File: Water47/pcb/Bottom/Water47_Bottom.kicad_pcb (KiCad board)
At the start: 2 copper layers, 260 x 76.5 mm, 5 parts, among them U1 MOUDLE-SEEEDUINO-XIAO

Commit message: feat: change mounting spacer to hex
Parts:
- H1, H2, H3, H4: footprint kbd_Hole:m2_Screw_Hole -> kbd_Hole:m2_Spacer_Hole_hex
- turned H1 to 90 degrees
- turned H2 to 90 degrees
- turned H3 to 90 degrees
- turned H4 to 90 degrees
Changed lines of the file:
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@@
       (net 13 "+5V") (pinfunction "5V") (pintype "passive"))
   )
-  (footprint "kbd_Hole:m2_Screw_Hole" (layer "F.Cu")
-    (at 85 87.2)
-    (descr "Mounting Hole 2.2mm, no annular, M2")
-    (tags "mounting hole 2.2mm no annular m2")
-    (property "Sheetfile" "Water47_Bottom.kicad_sch")
-    (property "Sheetname" "")
-    (autoplace_cost90 1)
-    (attr exclude_from_pos_files)
-    (fp_text reference "H1" (at 0 -3.2) (layer "F.Fab")
-      (effects (font (size 1 1) (thickness 0.15)))
-    )
-    (fp_text value "MountingHole" (at 0 3.2) (layer "F.Fab") hide
-      (effects (font (size 1 1) (thickness 0.15)))
-    )
-    (fp_text user "${REFERENCE}" (at 0.3 0) (layer "F.Fab") hide
-      (effects (font (size 1 1) (thickness 0.15)))
-    )
-    (fp_circle (center 0 0) (end 2.2 0) (layer "Cmts.User") (width 0.15) (fill none))
-    (fp_circle (center 0 0) (end 2.45 0) (layer "F.CrtYd") (width 0.05) (fill none))
-    (pad "" np_thru_hole circle locked (at 0 0) (size 2.2 2.2) (drill 2.2) (layers *.Cu *.Mask))
-  )
-  (footprint "kbd_Hole:m2_Screw_Hole" (layer "F.Cu")
-    (at 85 155.7)
+  (footprint "kbd_Hole:m2_Spacer_Hole_hex" (layer "F.Cu")
+    (at 85 87.2 90)
     (descr "Mounting Hole 2.2mm, no annular, M2")
     (tags "mounting hole 2.2mm no annular m2")
@@
     (property "Sheetname" "")
     (attr exclude_from_pos_files)
-    (fp_text reference "H2" (at 0 -3.2) (layer "F.Fab")
+    (fp_text reference "H1" (at 0 -3.2 90) (layer "F.Fab")
       (effects (font (size 1 1) (thickness 0.15)))
     )
-    (fp_text value "MountingHole" (at 0 3.2) (layer "F.Fab") hide
+    (fp_text value "MountingHole" (at 0 3.2 90) (layer "F.Fab")
       (effects (font (size 1 1) (thickness 0.15)))
     )
-    (fp_text user "${REFERENCE}" (at 0.3 0) (layer "F.Fab") hide
-      (effects (font (size 1 1) (thickness 0.15)))
-    )
-    (fp_circle (center 0 0) (end 2.2 0) (layer "Cmts.User") (width 0.15) (fill none))
-    (fp_circle (center 0 0) (end 2.45 0) (layer "F.CrtYd") (width 0.05) (fill none))
-    (pad "" np_thru_hole circle locked (at 0 0) (size 2.2 2.2) (drill 2.2) (layers *.Cu *.Mask))
+    (fp_line (start 1.2 -2.15) (end -1.2 -2.15) (layer "Edge.Cuts") (width 0.1))
+    (fp_line (start -1.2 2.15) (end 1.2 2.15) (layer "Edge.Cuts") (width 0.1))
+    (fp_line (start -1.2 -2.15) (end -2.4 0) (layer "Edge.Cuts") (width 0.1))
+    (fp_line (start -2.4 0) (end -1.2 2.15) (layer "Edge.Cuts") (width 0.1))
+    (fp_line (start 1.2 2.15) (end 2.4 0) (layer "Edge.Cuts") (width 0.1))
+    (fp_line (start 2.4 0) (end 1.2 -2.15) (layer "Edge.Cuts") (width 0.1))
   )
-  (footprint "kbd_Hole:m2_Screw_Hole" (layer "F.Cu")
-    (at 339 155.7)
+  (footprint "kbd_Hole:m2_Spacer_Hole_hex" (layer "F.Cu")
+    (at 85 155.7 90)
     (descr "Mounting Hole 2.2mm, no annular, M2")
     (tags "mounting hole 2.2mm no annular m2")
@@
     (property "Sheetname" "")
     (attr exclude_from_pos_files)
-    (fp_text reference "H4" (at 0 -3.2) (layer "F.Fab") hide
+    (fp_text reference "H2" (at 0 -3.2 90) (layer "F.Fab")
       (effects (font (size 1 1) (thickness 0.15)))
     )
-    (fp_text value "MountingHole" (at 0 3.2) (layer "F.Fab") hide
+    (fp_text value "MountingHole" (at 0 3.2 90) (layer "F.Fab")
       (effects (font (size 1 1) (thickness 0.15)))
     )
-    (fp_text user "${REFERENCE}" (at 0.3 0) (layer "F.Fab") hide
-      (effects (font (size 1 1) (thickness 0.15)))
-    )
-    (fp_circle (center 0 0) (end 2.2 0) (layer "Cmts.User") (width 0.15) (fill none))
-    (fp_circle (center 0 0) (end 2.45 0) (layer "F.CrtYd") (width 0.05) (fill none))
-    (pad "" np_thru_hole circle locked (at 0 0) (size 2.2 2.2) (drill 2.2) (layers *.Cu *.Mask))
+    (fp_line (start 1.2 -2.15) (end -1.2 -2.15) (layer "Edge.Cuts") (width 0.1))
+    (fp_line (start 1.2 2.15) (end 2.4 0) (layer "Edge.Cuts") (width 0.1))
+    (fp_line (start 2.4 0) (end 1.2 -2.15) (layer "Edge.Cuts") (width 0.1))
+    (fp_line (start -1.2 -2.15) (end -2.4 0) (layer "Edge.Cuts") (width 0.1))
+    (fp_line (start -1.2 2.15) (end 1.2 2.15) (layer "Edge.Cuts") (width 0.1))
+    (fp_line (start -2.4 0) (end -1.2 2.15) (layer "Edge.Cuts") (width 0.1))
   )
-  (footprint "kbd_Hole:m2_Screw_Hole" (layer "F.Cu")
-    (at 339 87.2)
+  (footprint "kbd_Hole:m2_Spacer_Hole_hex" (layer "F.Cu")
+    (at 339 155.7 90)
     (descr "Mounting Hole 2.2mm, no annular, M2")
     (tags "mounting hole 2.2mm no annular m2")
@@
     (property "Sheetname" "")
     (attr exclude_from_pos_files)
-    (fp_text reference "H3" (at 0 -3.2) (layer "F.Fab")
+    (fp_text reference "H4" (at 0 -3.2 90) (layer "F.Fab")
       (effects (font (size 1 1) (thickness 0.15)))
     )
-    (fp_text value "MountingHole" (at 0 3.2) (layer "F.Fab")
+    (fp_text value "MountingHole" (at 0 3.2 90) (layer "F.Fab")
       (effects (font (size 1 1) (thickness 0.15)))
     )
-    (fp_text user "${REFERENCE}" (at 0.3 0) (layer "F.Fab") hide
+    (fp_line (start 1.2 2.15) (end 2.4 0) (layer "Edge.Cuts") (width 0.1))
+    (fp_line (start 1.2 -2.15) (end -1.2 -2.15) (layer "Edge.Cuts") (width 0.1))
+    (fp_line (start -1.2 2.15) (end 1.2 2.15) (layer "Edge.Cuts") (width 0.1))
+    (fp_line (start 2.4 0) (end 1.2 -2.15) (layer "Edge.Cuts") (width 0.1))
+    (fp_line (start -1.2 -2.15) (end -2.4 0) (layer "Edge.Cuts") (width 0.1))
+    (fp_line (start -2.4 0) (end -1.2 2.15) (layer "Edge.Cuts") (width 0.1))
+  )
+  (footprint "kbd_Hole:m2_Spacer_Hole_hex" (layer "F.Cu")
+    (at 339 87.2 90)
+    (descr "Mounting Hole 2.2mm, no annular, M2")
+    (tags "mounting hole 2.2mm no annular m2")
+    (property "Sheetfile" "Water47_Bottom.kicad_sch")
+    (property "Sheetname" "")
+    (attr exclude_from_pos_files)
+    (fp_text reference "H3" (at 0 -3.2 90) (layer "F.Fab")
       (effects (font (size 1 1) (thickness 0.15)))
     )
-    (fp_circle (center 0 0) (end 2.2 0) (layer "Cmts.User") (width 0.15) (fill none))
-    (fp_circle (center 0 0) (end 2.45 0) (layer "F.CrtYd") (width 0.05) (fill none))
-    (pad "" np_thru_hole circle locked (at 0 0) (size 2.2 2.2) (drill 2.2) (layers *.Cu *.Mask))
+    (fp_text value "MountingHole" (at 0 3.2 90) (layer "F.Fab")
+      (effects (font (size 1 1) (thickness 0.15)))
+    )
+    (fp_line (start -1.2 -2.15) (end -2.4 0) (layer "Edge.Cuts") (width 0.1))
+    (fp_line (start -1.2 2.15) (end 1.2 2.15) (layer "Edge.Cuts") (width 0.1))
+    (fp_line (start -2.4 0) (end -1.2 2.15) (layer "Edge.Cuts") (width 0.1))
+    (fp_line (start 2.4 0) (end 1.2 -2.15) (layer "Edge.Cuts") (width 0.1))
+    (fp_line (start 1.2 -2.15) (end -1.2 -2.15) (layer "Edge.Cuts") (width 0.1))
+    (fp_line (start 1.2 2.15) (end 2.4 0) (layer "Edge.Cuts") (width 0.1))
   )
   (gr_line (start 340 83.2) (end 337.5 83.2) (layer "Edge.Cuts") (width 0.1))

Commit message: feat: change mounting hole
PCB : Hex
Others : Round
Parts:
- H1, H2, H3, H4: footprint kbd_Hole:m2_Spacer_Hole_hex -> kbd_Hole:m2_Screw_Hole
- turned H1 to 0 degrees
- turned H2 to 0 degrees
- turned H3 to 0 degrees
- turned H4 to 0 degrees
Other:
- board text added: "Water47 ver1.0 @Bottom Designed by multifeb13"
- board text removed: "Water47 ver1.0 @PCB Designed by multifeb13"
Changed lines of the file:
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@@
       (net 13 "+5V") (pinfunction "5V") (pintype "passive"))
   )
-  (footprint "kbd_Hole:m2_Spacer_Hole_hex" (layer "F.Cu")
-    (at 85 87.2 90)
+  (footprint "kbd_Hole:m2_Screw_Hole" (layer "F.Cu")
+    (at 85 87.2)
     (descr "Mounting Hole 2.2mm, no annular, M2")
     (tags "mounting hole 2.2mm no annular m2")
@@
     (property "Sheetname" "")
     (attr exclude_from_pos_files)
-    (fp_text reference "H1" (at 0 -3.2 90) (layer "F.Fab")
+    (fp_text reference "H1" (at 0 -3.2) (layer "F.Fab")
       (effects (font (size 1 1) (thickness 0.15)))
     )
-    (fp_text value "MountingHole" (at 0 3.2 90) (layer "F.Fab")
+    (fp_text value "MountingHole" (at 0 3.2) (layer "F.Fab")
       (effects (font (size 1 1) (thickness 0.15)))
     )
-    (fp_line (start 1.2 -2.15) (end -1.2 -2.15) (layer "Edge.Cuts") (width 0.1))
-    (fp_line (start -1.2 2.15) (end 1.2 2.15) (layer "Edge.Cuts") (width 0.1))
-    (fp_line (start -1.2 -2.15) (end -2.4 0) (layer "Edge.Cuts") (width 0.1))
-    (fp_line (start -2.4 0) (end -1.2 2.15) (layer "Edge.Cuts") (width 0.1))
-    (fp_line (start 1.2 2.15) (end 2.4 0) (layer "Edge.Cuts") (width 0.1))
-    (fp_line (start 2.4 0) (end 1.2 -2.15) (layer "Edge.Cuts") (width 0.1))
+    (fp_text user "${REFERENCE}" (at 0.3 0) (layer "F.Fab")
+      (effects (font (size 1 1) (thickness 0.15)))
+    )
+    (fp_circle (center 0 0) (end 2.2 0) (layer "Cmts.User") (width 0.15) (fill none))
+    (fp_circle (center 0 0) (end 2.45 0) (layer "F.CrtYd") (width 0.05) (fill none))
+    (pad "" np_thru_hole circle locked (at 0 0) (size 2.2 2.2) (drill 2.2) (layers *.Cu *.Mask))
   )
-  (footprint "kbd_Hole:m2_Spacer_Hole_hex" (layer "F.Cu")
-    (at 85 155.7 90)
+  (footprint "kbd_Hole:m2_Screw_Hole" (layer "F.Cu")
+    (at 85 155.7)
     (descr "Mounting Hole 2.2mm, no annular, M2")
     (tags "mounting hole 2.2mm no annular m2")
@@
     (property "Sheetname" "")
     (attr exclude_from_pos_files)
-    (fp_text reference "H2" (at 0 -3.2 90) (layer "F.Fab")
+    (fp_text reference "H2" (at 0 -3.2) (layer "F.Fab")
       (effects (font (size 1 1) (thickness 0.15)))
     )
-    (fp_text value "MountingHole" (at 0 3.2 90) (layer "F.Fab")
+    (fp_text value "MountingHole" (at 0 3.2) (layer "F.Fab")
       (effects (font (size 1 1) (thickness 0.15)))
     )
-    (fp_line (start 1.2 -2.15) (end -1.2 -2.15) (layer "Edge.Cuts") (width 0.1))
-    (fp_line (start 1.2 2.15) (end 2.4 0) (layer "Edge.Cuts") (width 0.1))
-    (fp_line (start 2.4 0) (end 1.2 -2.15) (layer "Edge.Cuts") (width 0.1))
-    (fp_line (start -1.2 -2.15) (end -2.4 0) (layer "Edge.Cuts") (width 0.1))
-    (fp_line (start -1.2 2.15) (end 1.2 2.15) (layer "Edge.Cuts") (width 0.1))
-    (fp_line (start -2.4 0) (end -1.2 2.15) (layer "Edge.Cuts") (width 0.1))
+    (fp_text user "${REFERENCE}" (at 0.3 0) (layer "F.Fab")
+      (effects (font (size 1 1) (thickness 0.15)))
+    )
+    (fp_circle (center 0 0) (end 2.2 0) (layer "Cmts.User") (width 0.15) (fill none))
+    (fp_circle (center 0 0) (end 2.45 0) (layer "F.CrtYd") (width 0.05) (fill none))
+    (pad "" np_thru_hole circle locked (at 0 0) (size 2.2 2.2) (drill 2.2) (layers *.Cu *.Mask))
   )
-  (footprint "kbd_Hole:m2_Spacer_Hole_hex" (layer "F.Cu")
-    (at 339 155.7 90)
+  (footprint "kbd_Hole:m2_Screw_Hole" (layer "F.Cu")
+    (at 339 155.7)
     (descr "Mounting Hole 2.2mm, no annular, M2")
     (tags "mounting hole 2.2mm no annular m2")
@@
     (property "Sheetname" "")
     (attr exclude_from_pos_files)
-    (fp_text reference "H4" (at 0 -3.2 90) (layer "F.Fab")
+    (fp_text reference "H4" (at 0 -3.2) (layer "F.Fab")
       (effects (font (size 1 1) (thickness 0.15)))
     )
-    (fp_text value "MountingHole" (at 0 3.2 90) (layer "F.Fab")
+    (fp_text value "MountingHole" (at 0 3.2) (layer "F.Fab")
       (effects (font (size 1 1) (thickness 0.15)))
     )
-    (fp_line (start 1.2 2.15) (end 2.4 0) (layer "Edge.Cuts") (width 0.1))
-    (fp_line (start 1.2 -2.15) (end -1.2 -2.15) (layer "Edge.Cuts") (width 0.1))
-    (fp_line (start -1.2 2.15) (end 1.2 2.15) (layer "Edge.Cuts") (width 0.1))
-    (fp_line (start 2.4 0) (end 1.2 -2.15) (layer "Edge.Cuts") (width 0.1))
-    (fp_line (start -1.2 -2.15) (end -2.4 0) (layer "Edge.Cuts") (width 0.1))
-    (fp_line (start -2.4 0) (end -1.2 2.15) (layer "Edge.Cuts") (width 0.1))
+    (fp_text user "${REFERENCE}" (at 0.3 0) (layer "F.Fab")
+      (effects (font (size 1 1) (thickness 0.15)))
+    )
+    (fp_circle (center 0 0) (end 2.2 0) (layer "Cmts.User") (width 0.15) (fill none))
+    (fp_circle (center 0 0) (end 2.45 0) (layer "F.CrtYd") (width 0.05) (fill none))
+    (pad "" np_thru_hole circle locked (at 0 0) (size 2.2 2.2) (drill 2.2) (layers *.Cu *.Mask))
   )
-  (footprint "kbd_Hole:m2_Spacer_Hole_hex" (layer "F.Cu")
-    (at 339 87.2 90)
+  (footprint "kbd_Hole:m2_Screw_Hole" (layer "F.Cu")
+    (at 339 87.2)
     (descr "Mounting Hole 2.2mm, no annular, M2")
     (tags "mounting hole 2.2mm no annular m2")
@@
     (property "Sheetname" "")
     (attr exclude_from_pos_files)
-    (fp_text reference "H3" (at 0 -3.2 90) (layer "F.Fab")
+    (fp_text reference "H3" (at 0 -3.2) (layer "F.Fab")
       (effects (font (size 1 1) (thickness 0.15)))
     )
-    (fp_text value "MountingHole" (at 0 3.2 90) (layer "F.Fab")
+    (fp_text value "MountingHole" (at 0 3.2) (layer "F.Fab")
       (effects (font (size 1 1) (thickness 0.15)))
     )
-    (fp_line (start -1.2 -2.15) (end -2.4 0) (layer "Edge.Cuts") (width 0.1))
-    (fp_line (start -1.2 2.15) (end 1.2 2.15) (layer "Edge.Cuts") (width 0.1))
-    (fp_line (start -2.4 0) (end -1.2 2.15) (layer "Edge.Cuts") (width 0.1))
-    (fp_line (start 2.4 0) (end 1.2 -2.15) (layer "Edge.Cuts") (width 0.1))
-    (fp_line (start 1.2 -2.15) (end -1.2 -2.15) (layer "Edge.Cuts") (width 0.1))
-    (fp_line (start 1.2 2.15) (end 2.4 0) (layer "Edge.Cuts") (width 0.1))
+    (fp_text user "${REFERENCE}" (at 0.3 0) (layer "F.Fab")
+      (effects (font (size 1 1) (thickness 0.15)))
+    )
+    (fp_circle (center 0 0) (end 2.2 0) (layer "Cmts.User") (width 0.15) (fill none))
+    (fp_circle (center 0 0) (end 2.45 0) (layer "F.CrtYd") (width 0.05) (fill none))
+    (pad "" np_thru_hole circle locked (at 0 0) (size 2.2 2.2) (drill 2.2) (layers *.Cu *.Mask))
   )
   (gr_line (start 340 83.2) (end 337.5 83.2) (layer "Edge.Cuts") (width 0.1))
@@
   (gr_arc (start 319 106.985786) (mid 317.585786 106.4) (end 317 104.985786) (layer "Edge.Cuts") (width 0.1))
   (gr_arc (start 84 159.7) (mid 82.585786 159.114214) (end 82 157.7) (layer "Edge.Cuts") (width 0.1))
-  (gr_text "Water47 ver1.0 @PCB Designed by multifeb13" (at 339 153 90) (layer "B.SilkS")
+  (gr_text "Water47 ver1.0 @Bottom Designed by multifeb13" (at 339 153 90) (layer "B.SilkS")
     (effects (font (size 1 1) (thickness 0.125)) (justify right mirror))
   )

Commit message: feat: add mounting holes
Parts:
- added H5: MountingHole, kbd_Hole:m2_Screw_Hole, F.Cu at (85.0, 104.8)
- added H6: MountingHole, kbd_Hole:m2_Screw_Hole, F.Cu at (339.0, 104.8)
- moved H2 263.1 mm to (339.0, 87.2)
- moved H3 263.1 mm to (85.0, 155.7)
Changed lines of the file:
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@@
   )
   (footprint "kbd_Hole:m2_Screw_Hole" (layer "F.Cu")
-    (at 85 155.7)
+    (at 339 87.2)
     (descr "Mounting Hole 2.2mm, no annular, M2")
     (tags "mounting hole 2.2mm no annular m2")
@@
     (attr exclude_from_pos_files)
     (fp_text reference "H2" (at 0 -3.2) (layer "F.Fab")
+      (effects (font (size 1 1) (thickness 0.15)))
+    )
+    (fp_text value "MountingHole" (at 0 3.2) (layer "F.Fab")
+      (effects (font (size 1 1) (thickness 0.15)))
+    )
+    (fp_text user "${REFERENCE}" (at 0.3 0) (layer "F.Fab")
+      (effects (font (size 1 1) (thickness 0.15)))
+    )
+    (fp_circle (center 0 0) (end 2.2 0) (layer "Cmts.User") (width 0.15) (fill none))
+    (fp_circle (center 0 0) (end 2.45 0) (layer "F.CrtYd") (width 0.05) (fill none))
+    (pad "" np_thru_hole circle locked (at 0 0) (size 2.2 2.2) (drill 2.2) (layers *.Cu *.Mask))
+  )
+  (footprint "kbd_Hole:m2_Screw_Hole" (layer "F.Cu")
+    (at 339 104.8)
+    (descr "Mounting Hole 2.2mm, no annular, M2")
+    (tags "mounting hole 2.2mm no annular m2")
+    (property "Sheetfile" "Water47_Bottom.kicad_sch")
+    (property "Sheetname" "")
+    (attr exclude_from_pos_files)
+    (fp_text reference "H6" (at 0 -3.2) (layer "F.Fab")
       (effects (font (size 1 1) (thickness 0.15)))
     )
@@
   )
   (footprint "kbd_Hole:m2_Screw_Hole" (layer "F.Cu")
-    (at 339 87.2)
+    (at 85 155.7)
     (descr "Mounting Hole 2.2mm, no annular, M2")
     (tags "mounting hole 2.2mm no annular m2")
@@
       (effects (font (size 1 1) (thickness 0.15)))
     )
+    (fp_text value "MountingHole" (at 0 3.2) (layer "F.Fab")
+      (effects (font (size 1 1) (thickness 0.15)))
+    )
+    (fp_text user "${REFERENCE}" (at 0.3 0) (layer "F.Fab")
+      (effects (font (size 1 1) (thickness 0.15)))
+    )
+    (fp_circle (center 0 0) (end 2.2 0) (layer "Cmts.User") (width 0.15) (fill none))
+    (fp_circle (center 0 0) (end 2.45 0) (layer "F.CrtYd") (width 0.05) (fill none))
+    (pad "" np_thru_hole circle locked (at 0 0) (size 2.2 2.2) (drill 2.2) (layers *.Cu *.Mask))
+  )
+  (footprint "kbd_Hole:m2_Screw_Hole" (layer "F.Cu")
+    (at 85 104.8)
+    (descr "Mounting Hole 2.2mm, no annular, M2")
+    (tags "mounting hole 2.2mm no annular m2")
+    (property "Sheetfile" "Water47_Bottom.kicad_sch")
+    (property "Sheetname" "")
+    (attr exclude_from_pos_files)
+    (fp_text reference "H5" (at 0 -3.2) (layer "F.Fab")
+      (effects (font (size 1 1) (thickness 0.15)))
+    )

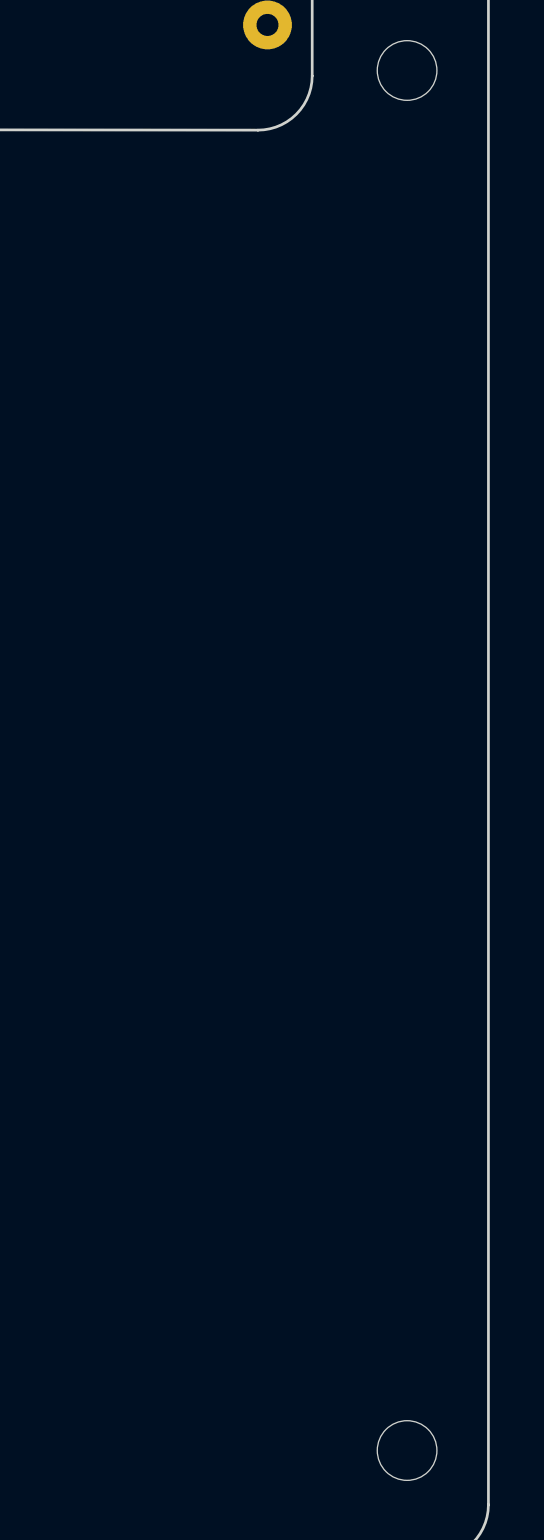
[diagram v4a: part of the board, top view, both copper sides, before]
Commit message: feat: add logo
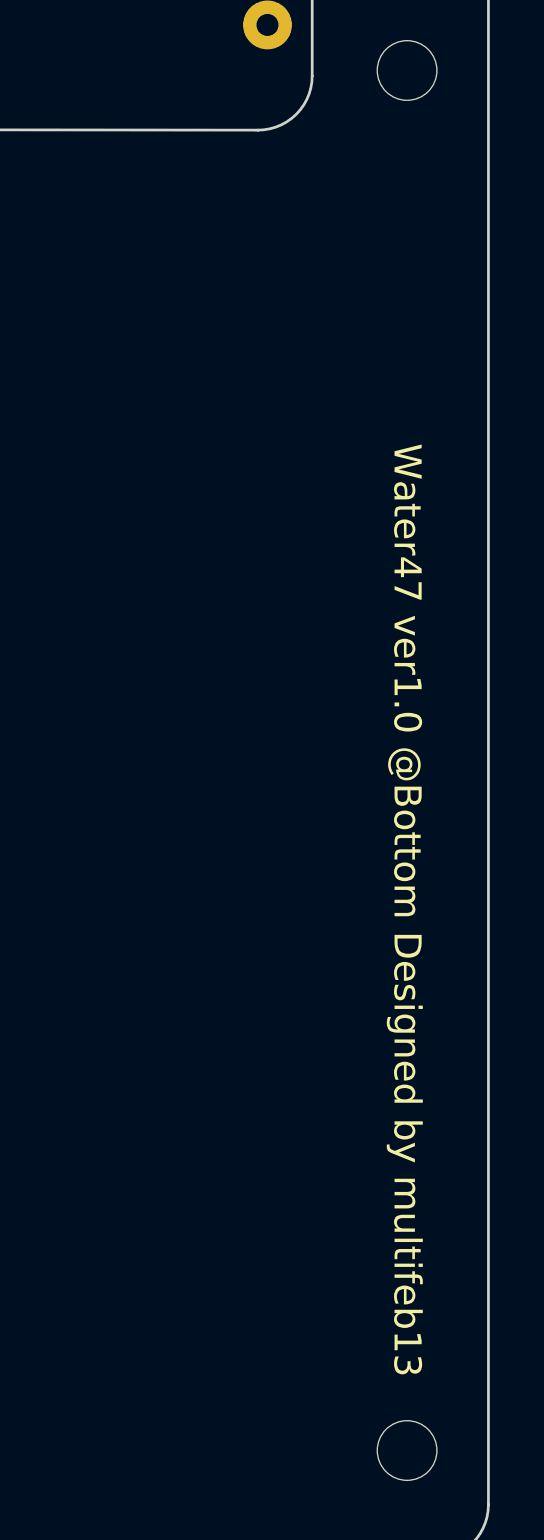
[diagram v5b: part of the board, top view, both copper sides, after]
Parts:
- added G***: LOGO, Silk_Wizard_logos:silk_wizard_logo_60x60, B.Cu at (212.0, 121.5)

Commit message: feat: increase logo size
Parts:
- G***: footprint Silk_Wizard_logos:silk_wizard_logo_60x60 -> Silk_Wizard_logos:silk_wizard_logo_70x70
